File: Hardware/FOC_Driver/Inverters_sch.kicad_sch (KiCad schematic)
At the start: 6 parts, among them Q4 CSD18540Q5B, Q5 CSD18540Q5B, Q6 CSD18540Q5B, Q7 CSD18540Q5B, Q8 CSD18540Q5B, Q9 CSD18540Q5B

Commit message: schematic updates
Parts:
- added C10, C12, C19, C20, C22, C23: 10u, Capacitor_SMD:C_1206_3216Metric, symbol Device:C
- added C18, C21, C24: 100n, Capacitor_SMD:C_0603_1608Metric, symbol Device:C
- added R14, R15, R3: 50m, Resistor_SMD:R_Shunt_Vishay_WSK2512_6332Metric_T1.19mm, symbol Device:R_Shunt
- added R16, R17, R18, R19, R20, R21: 10, eResistor:R_0603_1608Metric, symbol Device:R
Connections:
- net GHA: now also R16.1; no longer Q4.4 (G)
- net GHB: now also R18.1; no longer Q6.4 (G)
- net GHC: now also R20.1; no longer Q8.4 (G)
- net GLA: now also R17.1; no longer Q5.4 (G)
- net GLB: now also R19.1; no longer Q7.4 (G)
- net GLC: now also R21.1; no longer Q9.4 (G)
- net at Q9.1 (S), Q9.2 (S), Q9.3 (S): now also R15.1
- net at Q5.1 (S), Q5.2 (S), Q5.3 (S): now also R3.1
- net at Q7.1 (S), Q7.2 (S), Q7.3 (S): now also R14.1
- net VM renamed VBAT(+)
- net VBAT(+): now also C10.1, C12.1, C18.1, C19.1, C20.1, C21.1, C22.1, C23.1, C24.1
- new net: Q6.4 (G), R18.2
- new net: Q9.4 (G), R21.2
- new net: Q5.4 (G), R17.2
- new net: Q4.4 (G), R16.2
- new net: Q8.4 (G), R20.2
- new net: Q7.4 (G), R19.2
- new net GND: C10.2, C12.2, C18.2, C19.2, C20.2, C21.2, C22.2, C23.2, C24.2, R14.4, R15.4, R3.4
- new net SNA: R3.3
- new net SNB: R14.3
- new net SNC: R15.3
- new net SPA: R3.2
- new net SPB: R14.2
- new net SPC: R15.2
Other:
- note added: "Current sense: R_shunt = 50 mOhm, DRV8323 CSA gain = 10 V/V, VREF = 3.3 V Motor BGM5208-75T, 4S: I_max = (16.8 V / sqrt(3)) / 7.5 Ohm ≈ 1.3 A peak V_SO = VREF/2 + I x R_shunt x G = 1.65 V + I x 0.05 Ohm x 10 Full scale = 1.65 V / (G x R_shunt) = 1.65 V / (10 x 0.05 Ohm) = ±3.3 A (linear ≈ ±2.8 A) P_shunt = I² x R_shunt = (1.3 A)² x 0.05 Ohm ≈ 85 mW"
- moved on the sheet: Q4, Q5, Q6, Q7, Q8, Q9

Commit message: schematic completed
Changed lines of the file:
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@@
+		)
+	)
+	(label "VBAT(+)"
+		(at 138.43 46.99 0)
+		(effects
+			(font
+				(size 1.27 1.27)
+			)
+			(justify left bottom)
+		)
+	)
+	(label "VBAT(+)"
+		(at 208.28 46.99 0)
+		(effects
+			(font
+				(size 1.27 1.27)
+			)
+			(justify left bottom)
 		)
 	)
@@
 		)
 	)
-	(hierarchical_label "VBAT(+)"
-		(shape bidirectional)
-		(at 138.43 46.99 0)
-		(effects
-			(font
-				(size 1.27 1.27)
-			)
-			(justify left)
-		)
-	)
 	(hierarchical_label "SHB"
 		(shape bidirectional)
@@
 		(effects
 			(font
-				(size 1.27 1.27)
-			)
-			(justify left)
-		)
-	)
-	(hierarchical_label "VBAT(+)"
-		(shape bidirectional)
-		(at 208.28 46.99 0)
-		(effects
-			(font

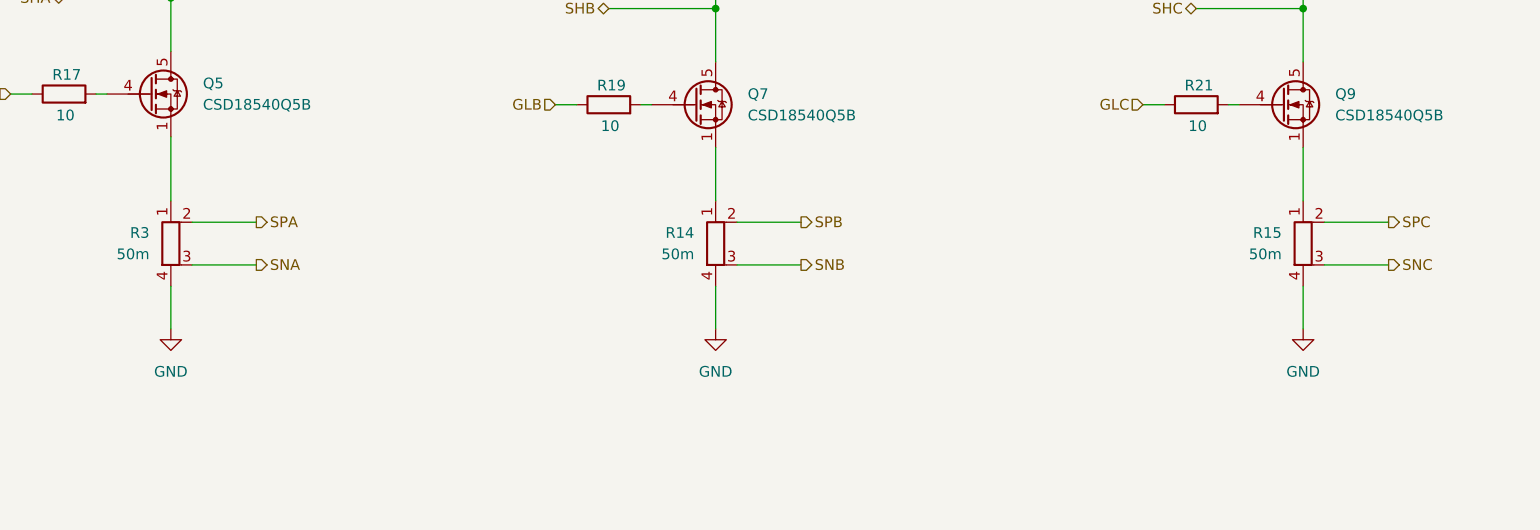
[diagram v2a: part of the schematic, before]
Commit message: Finished positioning and started layout v2
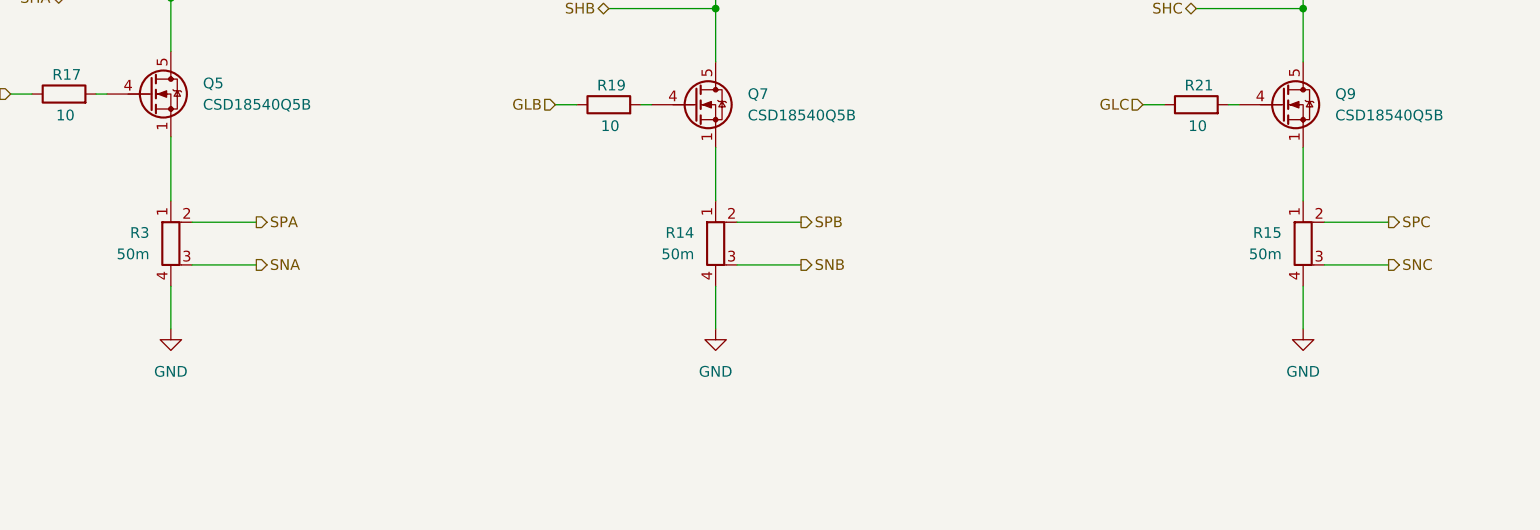
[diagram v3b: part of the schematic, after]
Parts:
- removed R14, R15, R3: 50m, Resistor_SMD:R_Shunt_Vishay_WSK2512_6332Metric_T1.19mm, symbol Device:R_Shunt
- added R14, R15, R3: 50m, eResistor:R_Shunt_Vishay_WSK2512_6332Metric_T1.19mm, symbol eResistor:R_shunt
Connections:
- net GND: now also R14.4, R15.4, R3.4
- net SNA: now also R3.3
- net SNB: now also R14.3
- net SNC: now also R15.3
- net SPA: now also R3.2
- net SPB: now also R14.2
- net SPC: now also R15.2
- net at Q5.1 (S), Q5.2 (S), Q5.3 (S): now also R3.1
- net at Q9.1 (S), Q9.2 (S), Q9.3 (S): now also R15.1
- net at Q7.1 (S), Q7.2 (S), Q7.3 (S): now also R14.1
